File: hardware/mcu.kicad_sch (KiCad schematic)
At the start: 20 parts, among them J1 Micro_SD_Card, SW8 BOOT, U1 ESP32-S3-WROOM-1, U10 PCA9555PW, U8 Ai-Thinker-Ra-02

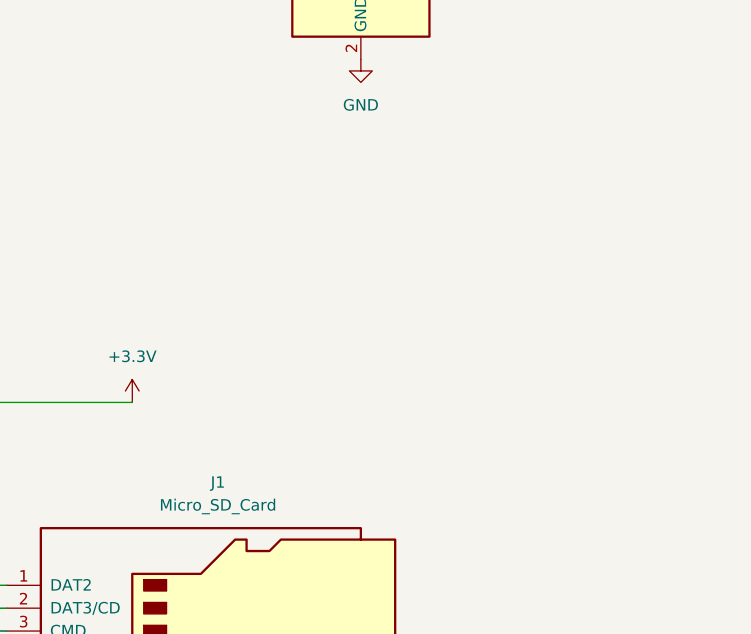
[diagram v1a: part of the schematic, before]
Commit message: add adafruit joystick
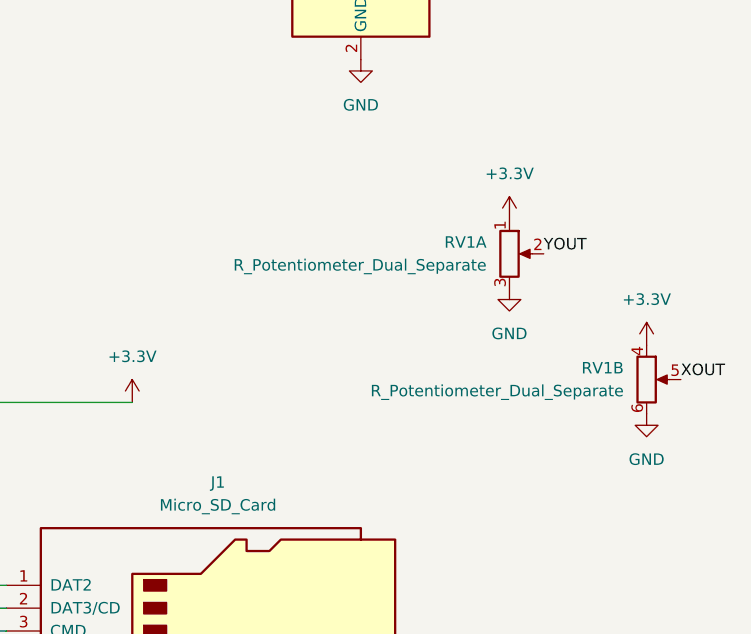
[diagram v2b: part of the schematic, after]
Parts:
- added RV1: R_Potentiometer_Dual_Separate, lib:JOYSTICK_ANALOG_MINITHM, symbol Device:R_Potentiometer_Dual_Separate
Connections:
- net +3.3V: now also RV1.1, RV1.4
- net GND: now also RV1.3, RV1.6
- new net XOUT: RV1.5
- new net YOUT: RV1.2

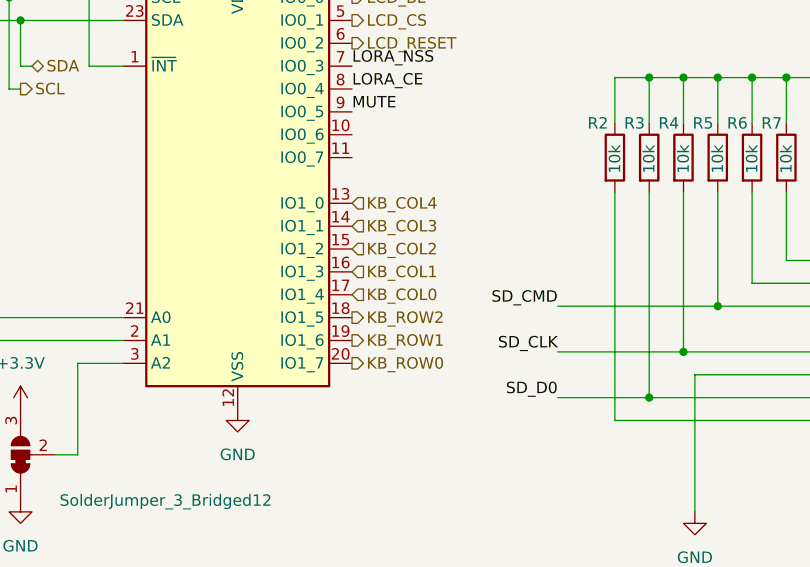
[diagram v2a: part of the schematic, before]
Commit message: remove mux, use i2c expander for keyboard
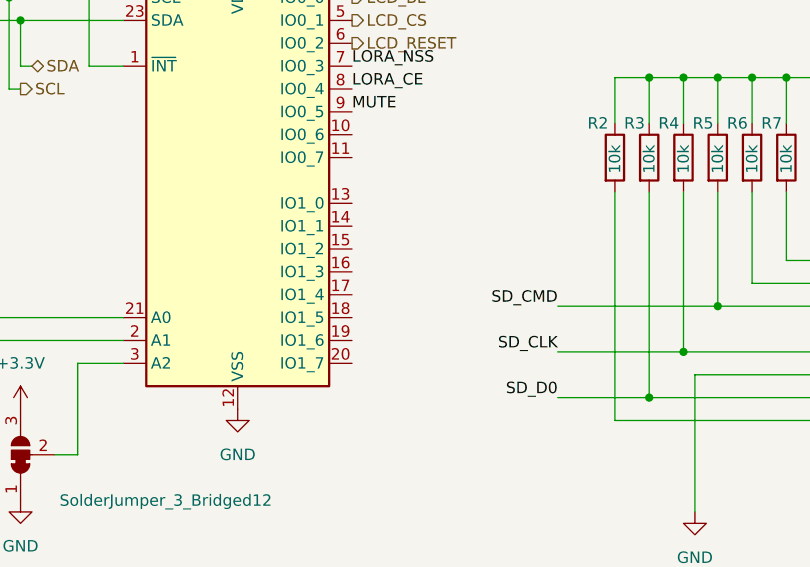
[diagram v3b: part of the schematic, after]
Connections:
- net KB_COL0: no longer names the net of U10.17 (IO1_4)
- net KB_COL1: no longer names the net of U10.16 (IO1_3)
- net KB_COL2: no longer names the net of U10.15 (IO1_2)
- net KB_COL3: no longer names the net of U10.14 (IO1_1)
- net KB_COL4: no longer names the net of U10.13 (IO1_0)
- net KB_ROW0: no longer names the net of U10.20 (IO1_7)
- net KB_ROW1: no longer names the net of U10.19 (IO1_6)
- net KB_ROW2: no longer names the net of U10.18 (IO1_5)
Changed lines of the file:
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@@
-		)
-	)
-	(hierarchical_label "KB_COL1"
-		(shape input)
-		(at 143.51 116.84 0)
-		(fields_autoplaced yes)
-		(effects
-			(font
-				(size 1.27 1.27)
-			)
-			(justify left)
-		)
-	)
-	(hierarchical_label "KB_ROW1"
-		(shape output)
-		(at 143.51 124.46 0)
-		(fields_autoplaced yes)
-		(effects
-			(font
-				(size 1.27 1.27)
-			)
-			(justify left)
 		)
 	)
@@
 		(shape output)
 		(at 143.51 86.36 0)
-		(fields_autoplaced yes)
-		(effects
-			(font
-				(size 1.27 1.27)
-			)
-			(justify left)
-		)
-	)
-	(hierarchical_label "KB_COL0"
-		(shape input)
-		(at 143.51 119.38 0)
 		(fields_autoplaced yes)
 		(effects
@@
 		)
 	)
-	(hierarchical_label "KB_ROW0"
-		(shape output)
-		(at 143.51 127 0)
-		(fields_autoplaced yes)
-		(effects
-			(font
-				(size 1.27 1.27)
-			)
-			(justify left)
-		)
-	)
 	(hierarchical_label "LCD_MISO"
 		(shape input)
@@
 		(shape output)
 		(at 143.51 88.9 0)
-		(fields_autoplaced yes)
-		(effects
-			(font
-				(size 1.27 1.27)
-			)
-			(justify left)
-		)
-	)
-	(hierarchical_label "KB_COL4"
-		(shape input)
-		(at 143.51 109.22 0)
-		(fields_autoplaced yes)
-		(effects
-			(font
-				(size 1.27 1.27)
-			)
-			(justify left)
-		)
-	)
-	(hierarchical_label "KB_ROW2"
-		(shape output)
-		(at 143.51 121.92 0)
 		(fields_autoplaced yes)
 		(effects
@@
 		(fields_autoplaced yes)
 		(effects
-			(font
-				(size 1.27 1.27)
-			)
-			(justify left)
-		)
-	)
-	(hierarchical_label "KB_COL3"
-		(shape input)
-		(at 143.51 111.76 0)
-		(fields_autoplaced yes)
-		(effects
-			(font
-				(size 1.27 1.27)
-			)
-			(justify left)
-		)
-	)
-	(hierarchical_label "KB_COL2"
-		(shape input)
-		(at 143.51 114.3 0)
-		(fields_autoplaced yes)
-		(effects

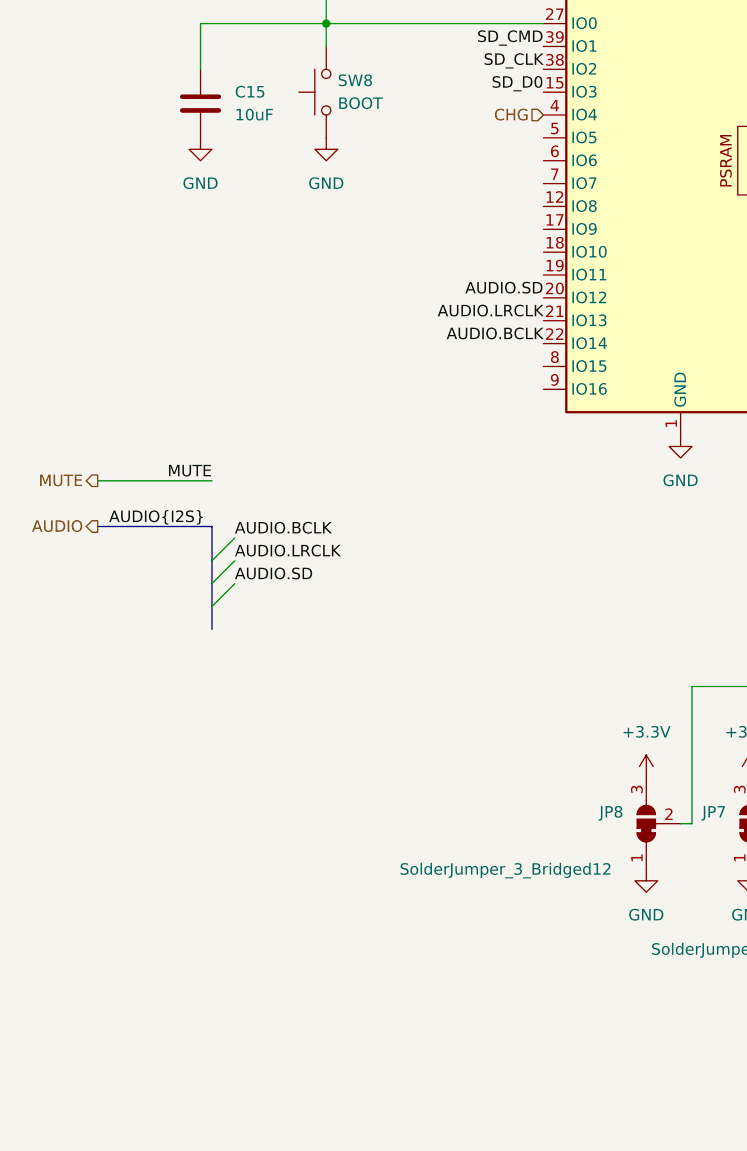
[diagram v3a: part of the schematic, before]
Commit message: add (analog) mems microphone
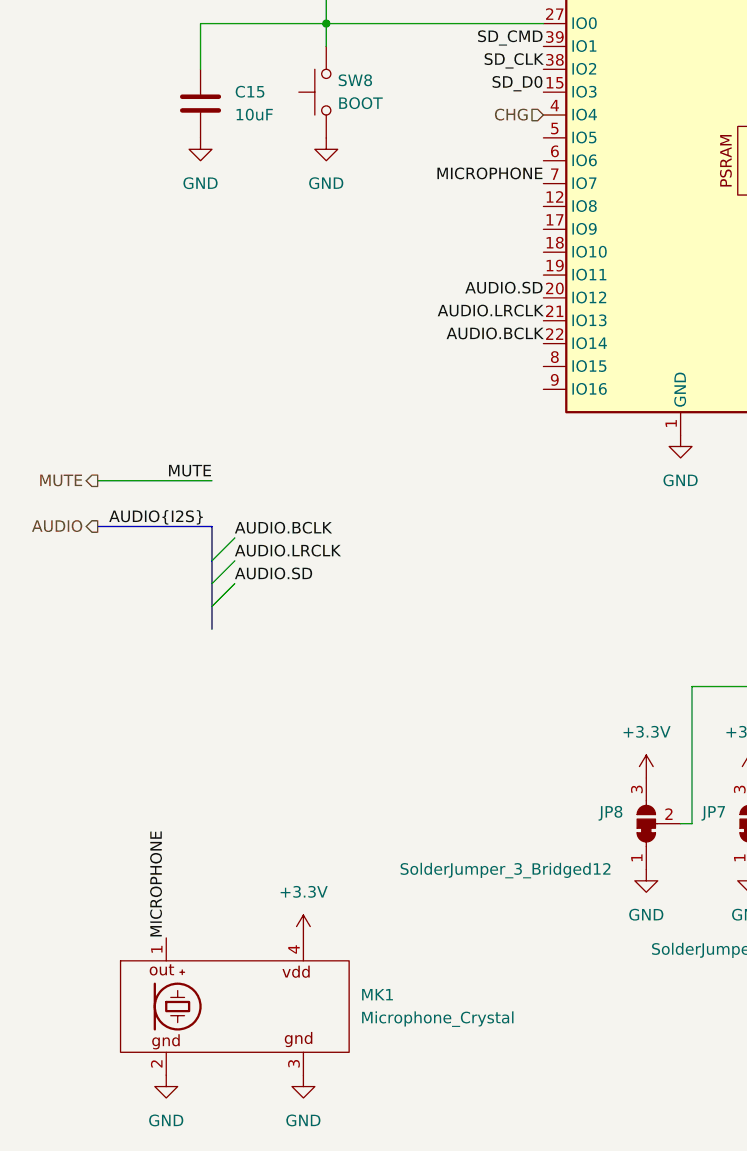
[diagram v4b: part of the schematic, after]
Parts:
- added MK1: Microphone_Crystal, lib:microfono, symbol microphone_crystal:Microphone_Crystal
- JP6: footprint (none) -> lib:microfono
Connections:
- net +3.3V: now also MK1.4 (-)
- net GND: now also MK1.2 (-), MK1.3 (-)
- net MICROPHONE: now reaches U1.7 (IO7)
- net MICROPHONE: now also MK1.1 (+)

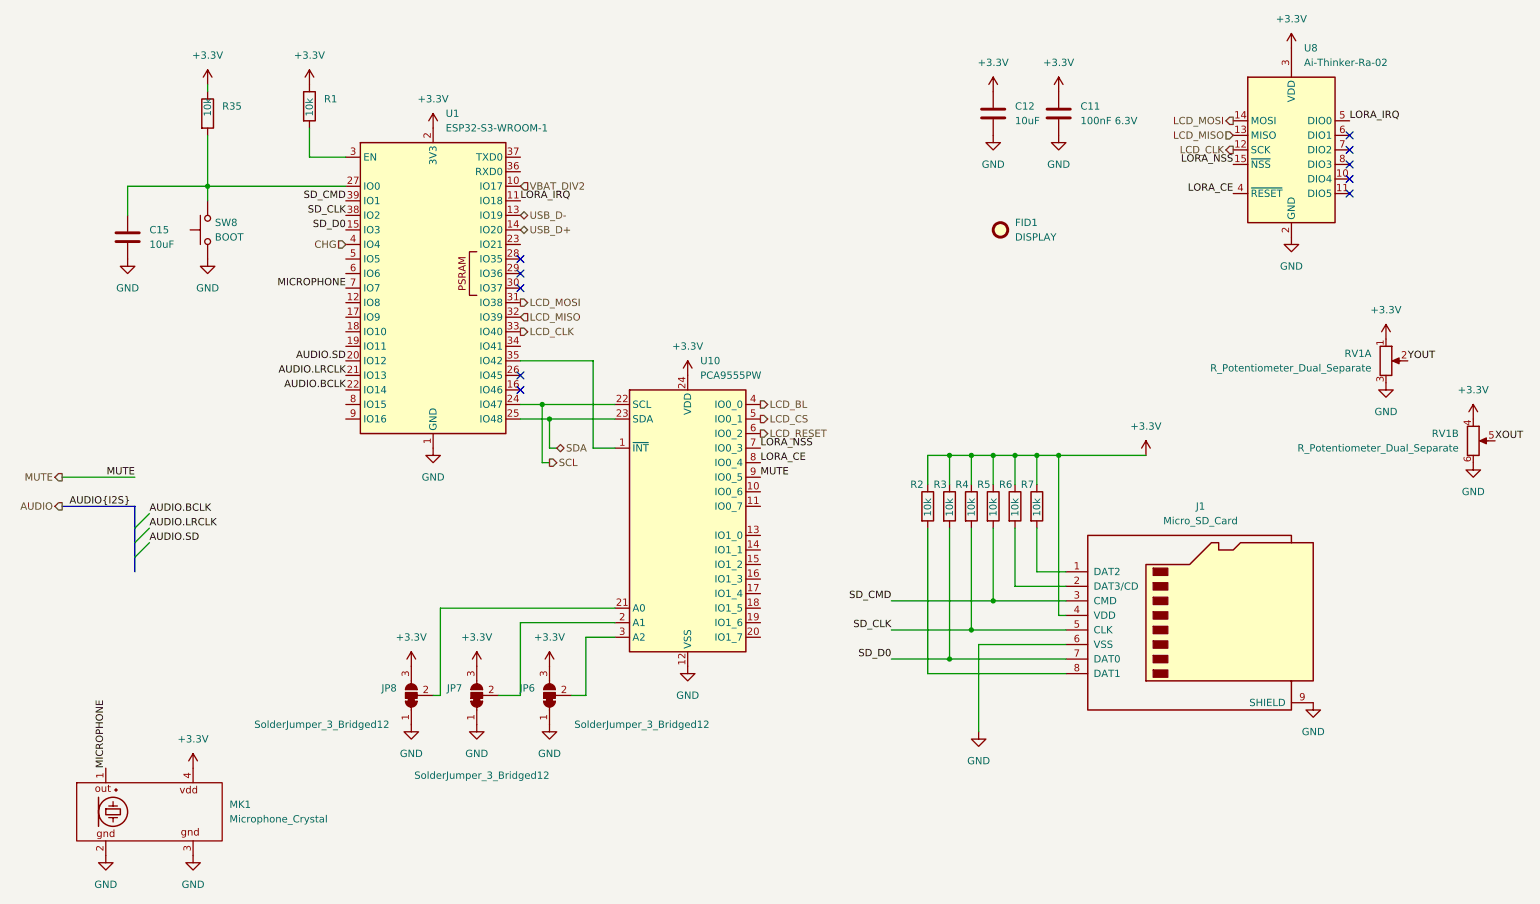
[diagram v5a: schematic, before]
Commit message: Create a preliminary routing
Disconnect the LORA module from the lcd bus
Add netclass and lenght matching rule for the LCD signals
Use Bus for spi syglas for easy netclass association
Remove cutaway jumper for the io expansions, and hardcode the address
Routed the keyboard matrix
Change the LCD resistor to 1202
Fix the0Ohm resistor footprint
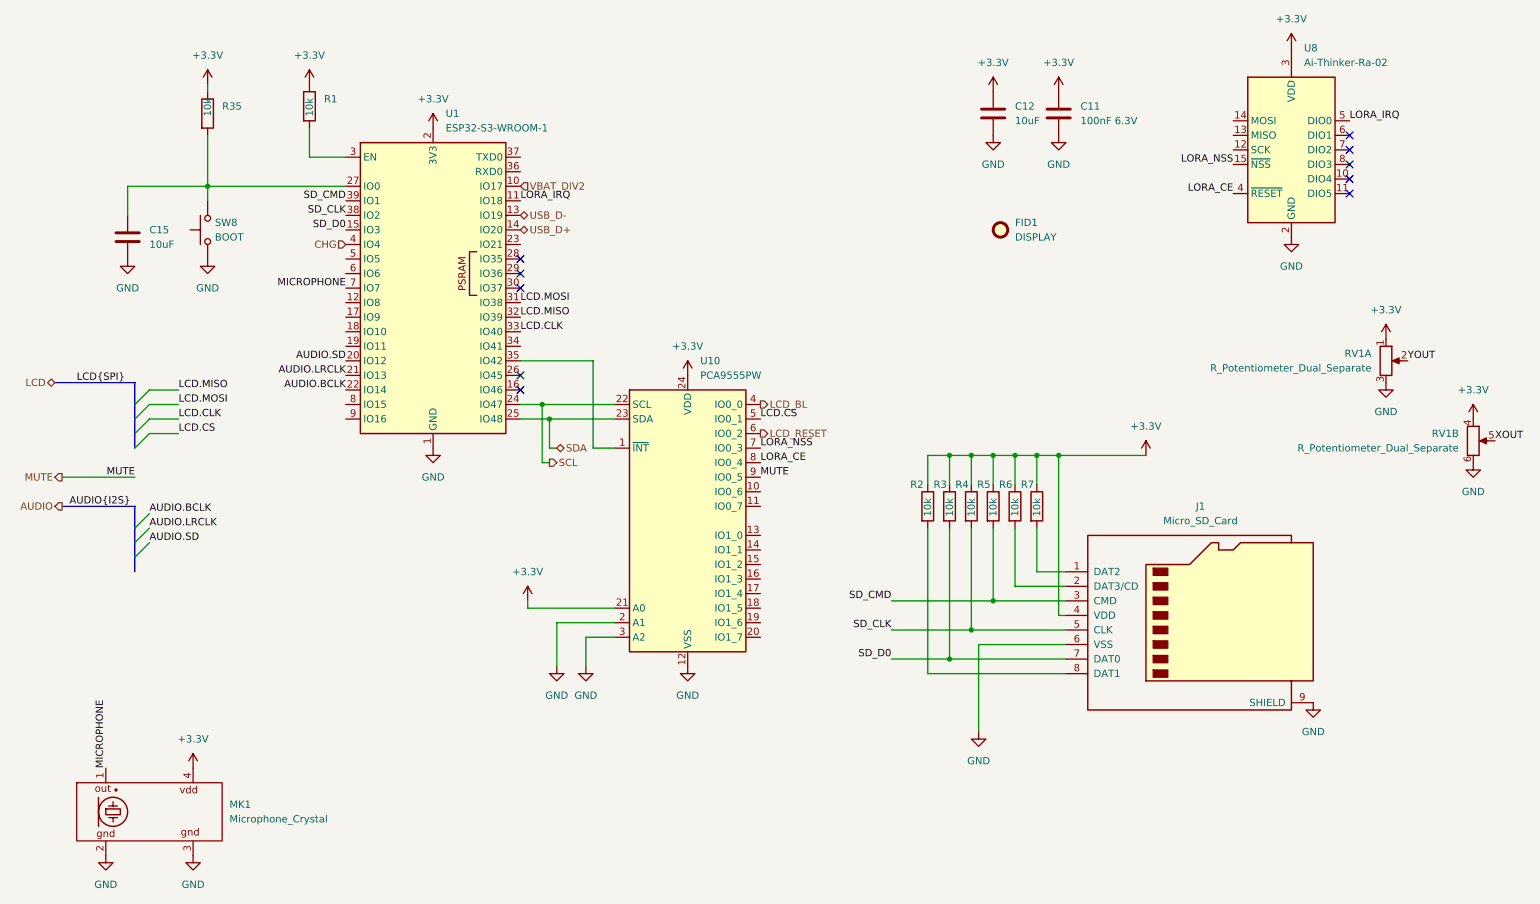
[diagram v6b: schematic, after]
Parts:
- removed JP6: SolderJumper_3_Bridged12, lib:microfono, symbol Jumper:SolderJumper_3_Bridged12
- removed JP7, JP8: SolderJumper_3_Bridged12, symbol Jumper:SolderJumper_3_Bridged12
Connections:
- net +3.3V: now also U10.21 (A0)
- net GND: now also U10.2 (A1), U10.3 (A2)
- net LCD_CLK: no longer names the net of U8.12 (SCK)
- net LCD_CLK: no longer U1.33 (IO40)
- net LCD_CS renamed LCD.CS
- net LCD_MISO: no longer names the net of U8.13 (MISO)
- net LCD_MISO: no longer U1.32 (IO39)
- net LCD_MOSI: no longer names the net of U8.14 (MOSI)
- net LCD_MOSI: no longer U1.31 (IO38)
- new net LCD.CLK: U1.33 (IO40)
- new net LCD.MISO: U1.32 (IO39)
- new net LCD.MOSI: U1.31 (IO38)

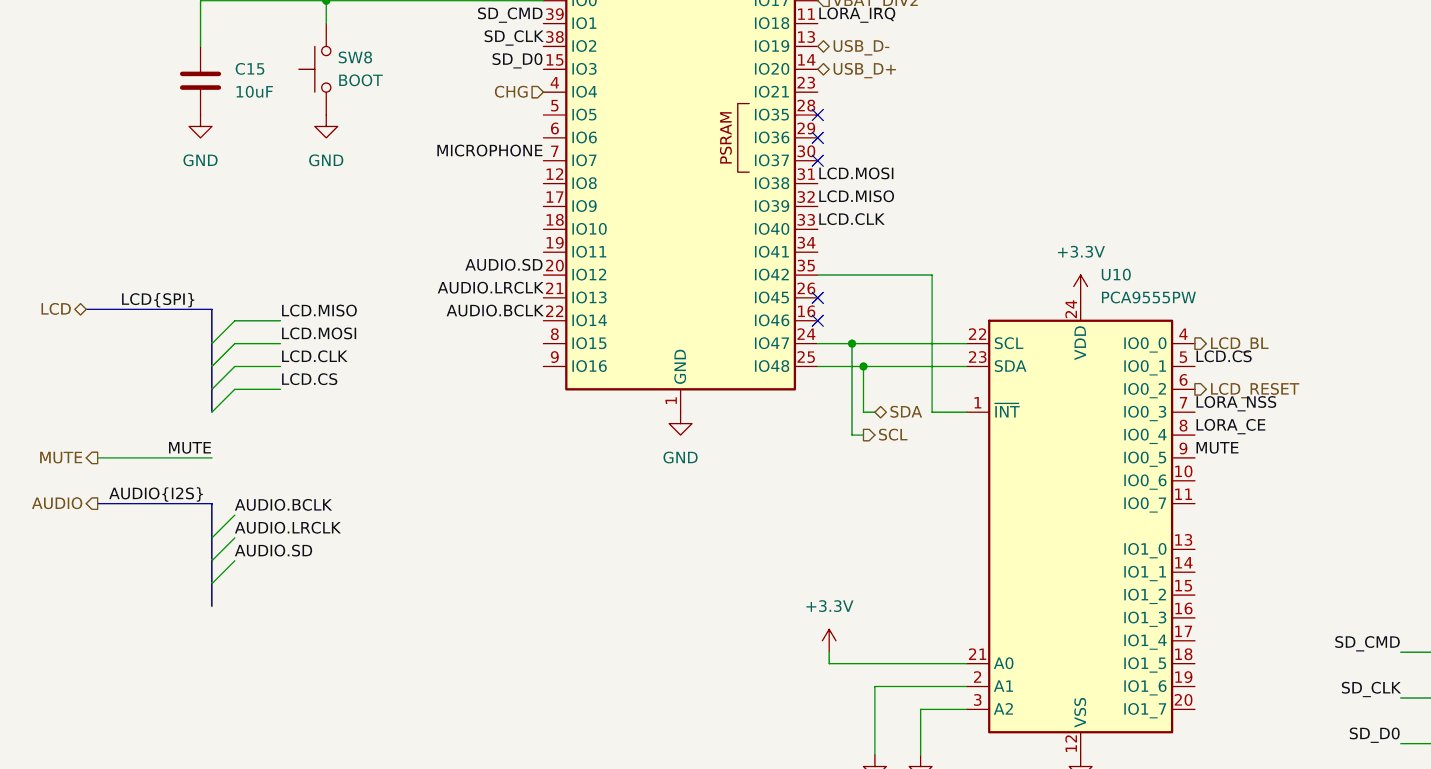
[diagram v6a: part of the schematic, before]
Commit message: Move usb to the opposite side of the PCB
Change the lcd SPI pins and use ones dirrectly atatched to SPI2
Lengh tune the LCD spi line and USB
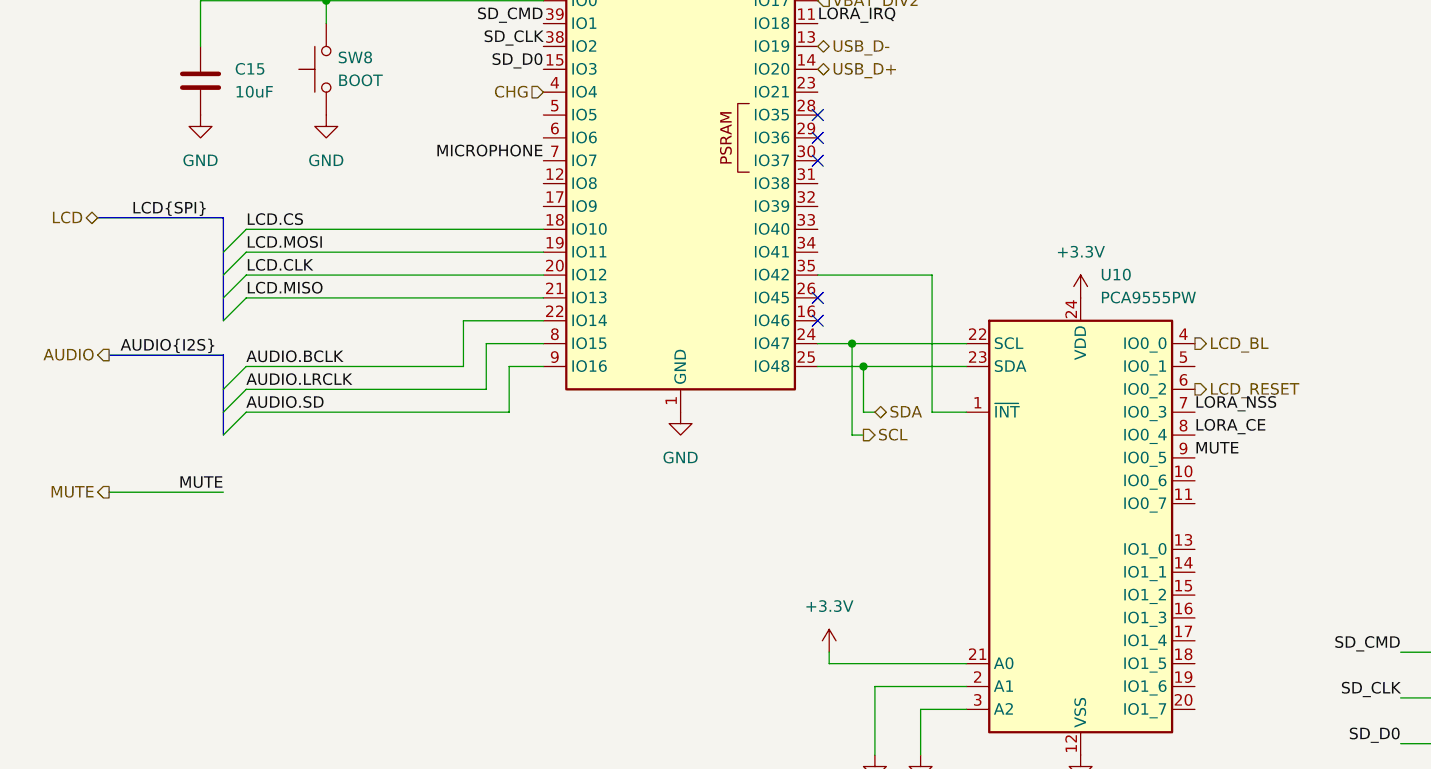
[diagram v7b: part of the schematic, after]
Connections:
- net AUDIO.LRCLK: now also U1.8 (IO15); no longer U1.21 (IO13)
- net AUDIO.SD: now also U1.9 (IO16); no longer U1.20 (IO12)
- net LCD.CLK: now also U1.20 (IO12); no longer U1.33 (IO40)
- net LCD.CS: now also U1.18 (IO10); no longer U10.5 (IO0_1)
- net LCD.MISO: now also U1.21 (IO13); no longer U1.32 (IO39)
- net LCD.MOSI: now also U1.19 (IO11); no longer U1.31 (IO38)
